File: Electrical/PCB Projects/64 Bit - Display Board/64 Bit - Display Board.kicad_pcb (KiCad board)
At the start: 4 copper layers, 200 x 75.1 mm, 60 parts, among them J1 Conn_01x03, J2 Conn_01x03, P1 610110249121, P2 610110249121, P3 610110249121, T1 IN-12A, T10 IN-12A, T2 IN-12A, T5 IN-12A, T6 IN-12A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

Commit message: slight changes
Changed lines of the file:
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@@
+	)
+	(segment
+		(start 106.5 56.5)
+		(end 95.9 56.5)
+		(width 0.3)
+		(layer "F.Cu")
+		(net 72)
+	)
+	(segment
+		(start 93.1 59.3)
+		(end 93.1 64.1)
+		(width 0.3)
+		(layer "F.Cu")
+		(net 72)
+	)
+	(segment
+		(start 117.5 96.1)
+		(end 112.1 90.7)
+		(width 0.3)
+		(layer "F.Cu")
+		(net 72)
+	)
+	(segment
+		(start 112.1 62.1)
+		(end 106.5 56.5)
+		(width 0.3)
+		(layer "F.Cu")
+		(net 72)
+	)
+	(segment
+		(start 112.1 90.7)
+		(end 112.1 62.1)
+		(width 0.3)
+		(layer "F.Cu")
+		(net 72)
+	)
+	(segment
+		(start 121.567267 92.442808)
+		(end 121.567267 92.432733)
+		(width 0.3)
+		(layer "F.Cu")
+		(net 72)
 	)
 	(segment
@@
 	)
 	(segment
-		(start 117.5 96.1)
-		(end 112.1 90.7)
-		(width 0.3)
-		(layer "F.Cu")
-		(net 72)
-	)
-	(segment
-		(start 93.1 59.3)
-		(end 93.1 64.1)
-		(width 0.3)
-		(layer "F.Cu")
-		(net 72)
-	)
-	(segment
-		(start 112.1 62.1)
-		(end 106.2 56.2)
-		(width 0.3)
-		(layer "F.Cu")
-		(net 72)
-	)
-	(segment
-		(start 96.2 56.2)
+		(start 95.9 56.5)
 		(end 93.1 59.3)
-		(width 0.3)
-		(layer "F.Cu")
-		(net 72)
-	)
-	(segment
-		(start 121.567267 92.442808)
-		(end 121.567267 92.432733)
-		(width 0.3)
-		(layer "F.Cu")
-		(net 72)
-	)
-	(segment
-		(start 112.1 90.7)
-		(end 112.1 62.1)
-		(width 0.3)
-		(layer "F.Cu")
-		(net 72)
-	)
-	(segment
-		(start 106.2 56.2)
-		(end 96.2 56.2)
 		(width 0.3)
 		(layer "F.Cu")
@@
 	)
 	(segment
+		(start 91 58.9)
+		(end 91 66.5)
+		(width 0.3)
+		(layer "F.Cu")
+		(net 79)
+	)
+	(segment
+		(start 114.1 90.5)
+		(end 114.1 60.9)
+		(width 0.3)
+		(layer "F.Cu")
+		(net 79)
+	)
+	(segment
 		(start 91 66.5)
 		(end 94 69.5)
@@
 	)
 	(segment
+		(start 108.40569 55.20569)
+		(end 94.69431 55.20569)
+		(width 0.3)
+		(layer "F.Cu")
+		(net 79)
+	)
+	(segment
+		(start 114.1 60.9)
+		(end 108.40569 55.20569)
+		(width 0.3)
+		(layer "F.Cu")
+		(net 79)
+	)
+	(segment
 		(start 119.4 95.8)
 		(end 114.1 90.5)
@@
 	)
 	(segment
-		(start 107.9 54.7)
-		(end 95.2 54.7)
-		(width 0.3)
-		(layer "F.Cu")
-		(net 79)
-	)
-	(segment
-		(start 95.2 54.7)
-		(end 91 58.9)
-		(width 0.3)
-		(layer "F.Cu")
-		(net 79)
-	)
-	(segment
-		(start 91 58.9)
-		(end 91 66.5)
-		(width 0.3)
-		(layer "F.Cu")
-		(net 79)
-	)
-	(segment
 		(start 122.559167 93.340833)
 		(end 124 91.9)
@@
 	)
 	(segment
-		(start 114.1 90.5)
-		(end 114.1 60.9)
-		(width 0.3)
-		(layer "F.Cu")
-		(net 79)
-	)
-	(segment
-		(start 114.1 60.9)
-		(end 107.9 54.7)
+		(start 94.69431 55.20569)
+		(end 91 58.9)
 		(width 0.3)
 		(layer "F.Cu")
@@
 	)
 	(segment
+		(start 116 90.2)
+		(end 116 58.8)
+		(width 0.3)
+		(layer "F.Cu")
+		(net 80)
+	)
+	(segment
 		(start 120.811072 95.011072)
 		(end 116 90.2)
@@
 	)
 	(segment
-		(start 93.328049 53.471951)
+		(start 116 58.8)
+		(end 111.2 54)
+		(width 0.3)
+		(layer "F.Cu")
+		(net 80)
+	)
+	(segment
+		(start 111.2 54)
+		(end 92.8 54)
+		(width 0.3)
+		(layer "F.Cu")
+		(net 80)
+	)
+	(segment
+		(start 92.8 54)
 		(end 89.5 57.3)
 		(width 0.3)
@@
 	)
 	(segment
-		(start 110.671951 53.471951)
-		(end 93.328049 53.471951)
+		(start 89.5 69.5)
+		(end 94 74)
+		(width 0.3)
+		(layer "F.Cu")
+		(net 80)
+	)
+	(segment
+		(start 89.5 57.3)
+		(end 89.5 69.5)
 		(width 0.3)
 		(layer "F.Cu")
@@
 	)
 	(segment
-		(start 89.5 69.5)
-		(end 94 74)
-		(width 0.3)
-		(layer "F.Cu")
-		(net 80)
-	)
-	(segment
 		(start 122.591105 95.011072)
 		(end 120.811072 95.011072)
-		(width 0.3)
-		(layer "F.Cu")
-		(net 80)
-	)
-	(segment
-		(start 89.5 57.3)
-		(end 89.5 69.5)
-		(width 0.3)
-		(layer "F.Cu")
-		(net 80)
-	)
-	(segment
-		(start 116 90.2)
-		(end 116 58.8)
-		(width 0.3)
-		(layer "F.Cu")
-		(net 80)
-	)
-	(segment
-		(start 116 58.8)
-		(end 110.671951 53.471951)
 		(width 0.3)
 		(layer "F.Cu")
@@
 		(net 2)
 		(net_name "GND")
-		(layers "F.Cu" "B.Cu")
+		(layers "F.Cu" "B.Cu" "In1.Cu")
 		(hatch edge 0.5)
 		(priority 1)
@@
 		(net 2)
 		(net_name "GND")
-		(layers "F.Cu" "B.Cu")
+		(layers "F.Cu" "B.Cu" "In1.Cu")
 		(hatch edge 0.5)
 		(priority 1)
@@
 		(net 2)
 		(net_name "GND")
-		(layers "F.Cu" "B.Cu")
+		(layers "F.Cu" "B.Cu" "In1.Cu")
 		(hatch edge 0.5)
 		(priority 1)
@@
 		(net 2)
 		(net_name "GND")
-		(layers "F.Cu" "B.Cu")
+		(layers "F.Cu" "B.Cu" "In1.Cu")
 		(hatch edge 0.5)
 		(priority 1)
@@
 		(net 2)
 		(net_name "GND")
-		(layers "F.Cu" "B.Cu")
+		(layers "F.Cu" "B.Cu" "In1.Cu")
 		(hatch edge 0.5)
 		(priority 1)

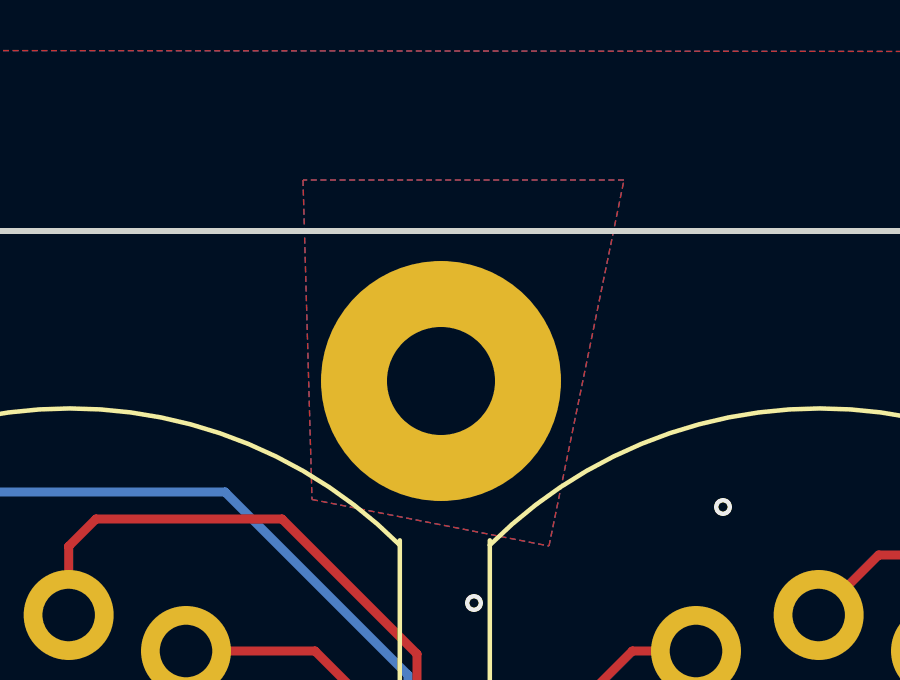
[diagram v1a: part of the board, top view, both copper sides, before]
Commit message: final. PCB outputs generated, ordering prototypes
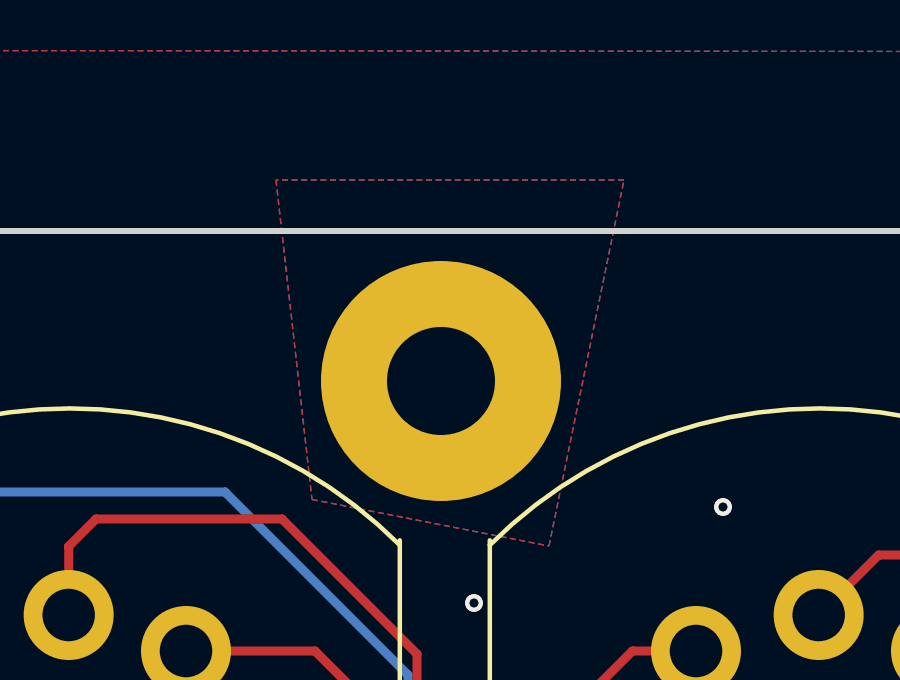
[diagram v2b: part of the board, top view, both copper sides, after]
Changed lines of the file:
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@@
 			(drillshape 0)
 			(scaleselection 1)
-			(outputdirectory "C:/Users/Kadin/Desktop/Git Projects/64-Bit/Electrical/PCB Outputs/64 Bit - Display Board/gerbers/")
+			(outputdirectory "C:/Users/kwhit/Desktop/projects/64-Bit/Electrical/PCB Outputs/64 Bit - Display Board/Gerbers/")
 		)
 	)
@@
 		(net 2)
 		(net_name "GND")
-		(layers "F.Cu" "B.Cu" "In1.Cu")
+		(layers "F.Cu" "B.Cu" "In1.Cu" "In2.Cu")
 		(hatch edge 0.5)
 		(priority 1)
@@
 		(net 2)
 		(net_name "GND")
-		(layers "F.Cu" "B.Cu" "In1.Cu")
+		(layers "F.Cu" "B.Cu" "In1.Cu" "In2.Cu")
 		(hatch edge 0.5)
-		(priority 1)
-		(connect_pads yes
-			(clearance 0.5)
+		(connect_pads
+			(clearance 1)
 		)
 		(min_thickness 0.25)
@@
 		(polygon
 			(pts
-				(xy 152.6 58) (xy 155.1 45.8) (xy 144.4 45.8) (xy 144.7 56.45)
+				(xy 44.8 41.4) (xy 253 41.6) (xy 252.8 127) (xy 44.5 127.2)
 			)
 		)
@@
 		(net 2)
 		(net_name "GND")
-		(layers "F.Cu" "B.Cu" "In1.Cu")
+		(layers "F.Cu" "B.Cu" "In1.Cu" "In2.Cu")
 		(hatch edge 0.5)
 		(priority 1)
@@
 		(polygon
 			(pts
-				(xy 59.5 124.1) (xy 59.5 107.7) (xy 47.8 107.7) (xy 47.8 124.1)
+				(xy 152.6 58) (xy 155.1 45.8) (xy 143.5 45.8) (xy 144.7 56.45)
 			)
 		)
@@
 		(net 2)
 		(net_name "GND")
-		(layers "F.Cu" "B.Cu" "In1.Cu")
+		(layers "F.Cu" "B.Cu" "In1.Cu" "In2.Cu")
 		(hatch edge 0.5)
 		(priority 1)
@@
 		(polygon
 			(pts
-				(xy 250.5 56.9) (xy 250.5 46) (xy 239.05 46) (xy 239.05 56.9)
+				(xy 59.5 124.1) (xy 59.5 107.7) (xy 47.8 107.7) (xy 47.8 124.1)
 			)
 		)
@@
 		(net 2)
 		(net_name "GND")
-		(layers "F.Cu" "B.Cu" "In1.Cu")
+		(layers "F.Cu" "B.Cu" "In1.Cu" "In2.Cu")
 		(hatch edge 0.5)
 		(priority 1)
@@
 		(polygon
 			(pts
-				(xy 59.2 57.7) (xy 59.2 46.2) (xy 47.5 46.2) (xy 47.5 57.7)
+				(xy 250.5 56.9) (xy 250.5 46) (xy 239.05 46) (xy 239.05 56.9)
 			)
 		)
@@
 		(layers "F.Cu" "B.Cu" "In1.Cu" "In2.Cu")
 		(hatch edge 0.5)
-		(connect_pads
-			(clearance 1)
+		(priority 1)
+		(connect_pads yes
+			(clearance 0.5)
 		)
 		(min_thickness 0.25)
@@
 		(polygon
 			(pts
-				(xy 44.8 41.4) (xy 253 41.6) (xy 252.8 127) (xy 44.5 127.2)
+				(xy 59.2 57.7) (xy 59.2 46.2) (xy 47.5 46.2) (xy 47.5 57.7)
 			)
 		)
